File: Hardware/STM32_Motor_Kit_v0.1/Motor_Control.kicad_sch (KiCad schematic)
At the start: 138 parts, among them J4 Conn_01x03_Male, Q1 NTMFS4119NT1G, Q2 NTMFS4119NT1G, Q3 NTMFS4119NT1G, Q4 NTMFS4119NT1G, Q5 NTMFS4119NT1G, Q6 NTMFS4119NT1G, U10 LMV358IDRG4, U11 LMV358IDRG4, U12 LMV358IDRG4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

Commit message: Added GND polygon to Inner Layer-1
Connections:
- net +15V: now also JP5.2 (B), JP6.2 (B), JP7.2 (B); no longer JP5.1 (A), JP6.1 (A), JP7.1 (A)
- net at C44.1, C47.1, C50.1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: now also JP7.1 (A); no longer JP7.2 (B)
- net at C43.1, C46.1, C49.1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: now also JP6.1 (A); no longer JP6.2 (B)
- net at C45.1, C48.1, C51.1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: now also JP5.1 (A); no longer JP5.2 (B)
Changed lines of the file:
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@@
 		(lib_id "AKE_Device:Jumper_Pinheader")
 		(at 38.1 228.6 0)
+		(mirror y)
 		(unit 1)
 		(exclude_from_sim no)
@@
 		)
 		(property "Footprint" "AKE_Pinheader_TH:PinHeader_1x02_P2.54mm_Vertical"
-			(at 43.18 233.68 0)
+			(at 33.02 233.68 0)
 			(effects
 				(font
@@
 		(lib_id "AKE_Device:Jumper_Pinheader")
 		(at 39.37 165.1 0)
+		(mirror y)
 		(unit 1)
 		(exclude_from_sim no)
@@
 		)
 		(property "Footprint" "AKE_Pinheader_TH:PinHeader_1x02_P2.54mm_Vertical"
-			(at 44.45 170.18 0)
+			(at 34.29 170.18 0)
 			(effects
 				(font
@@
 		(lib_id "AKE_Device:Jumper_Pinheader")
 		(at 39.37 101.6 0)
+		(mirror y)
 		(unit 1)
 		(exclude_from_sim no)
@@
 		)
 		(property "Footprint" "AKE_Pinheader_TH:PinHeader_1x02_P2.54mm_Vertical"
-			(at 44.45 106.68 0)
+			(at 34.29 106.68 0)
 			(effects
 				(font

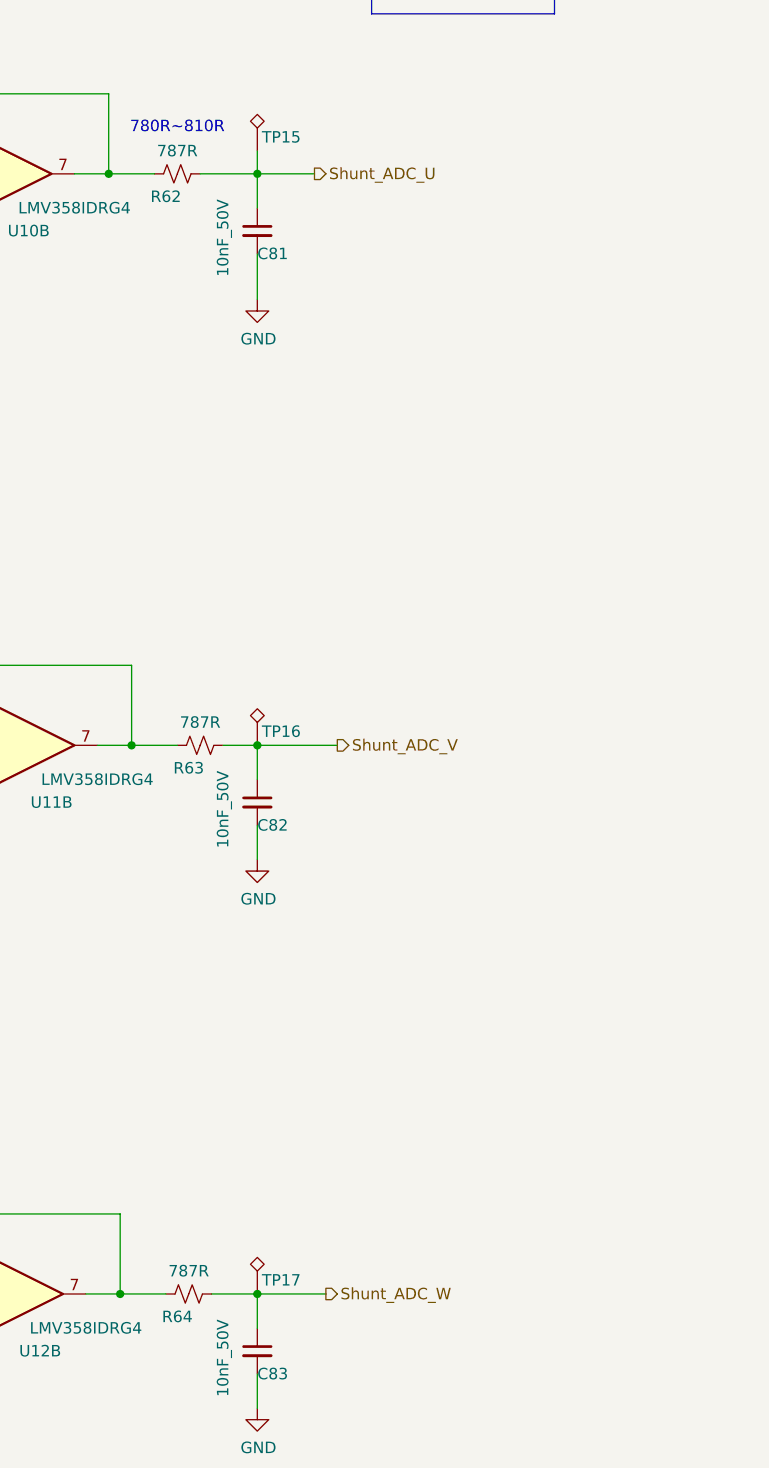
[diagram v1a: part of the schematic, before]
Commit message: Firmware Configuration added, Motor Control Pins and BackEMF Analog Pins setted.
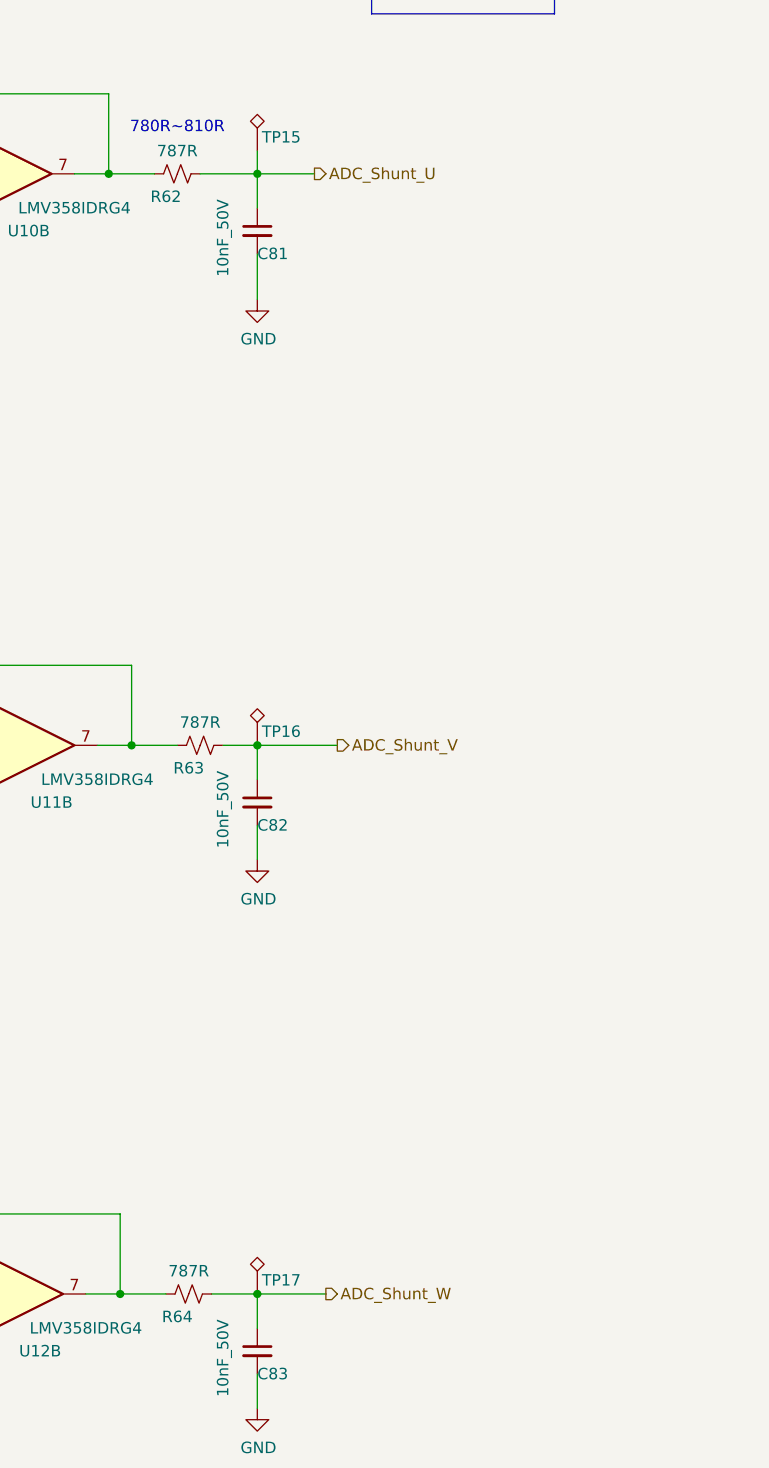
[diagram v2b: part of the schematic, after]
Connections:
- net Shunt_ADC_U renamed ADC_Shunt_U
- net Shunt_ADC_V renamed ADC_Shunt_V
- net Shunt_ADC_W renamed ADC_Shunt_W
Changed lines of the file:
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@@
 		)
 	)
-	(hierarchical_label "Shunt_ADC_V"
+	(hierarchical_label "ADC_Shunt_V"
 		(shape output)
 		(at 363.22 172.72 0)
@@
 		)
 	)
-	(hierarchical_label "Shunt_ADC_W"
+	(hierarchical_label "ADC_Shunt_W"
 		(shape output)
 		(at 361.95 233.68 0)
@@
 		)
 	)
-	(hierarchical_label "Shunt_ADC_U"
+	(hierarchical_label "ADC_Shunt_U"
 		(shape output)
 		(at 360.68 109.22 0)

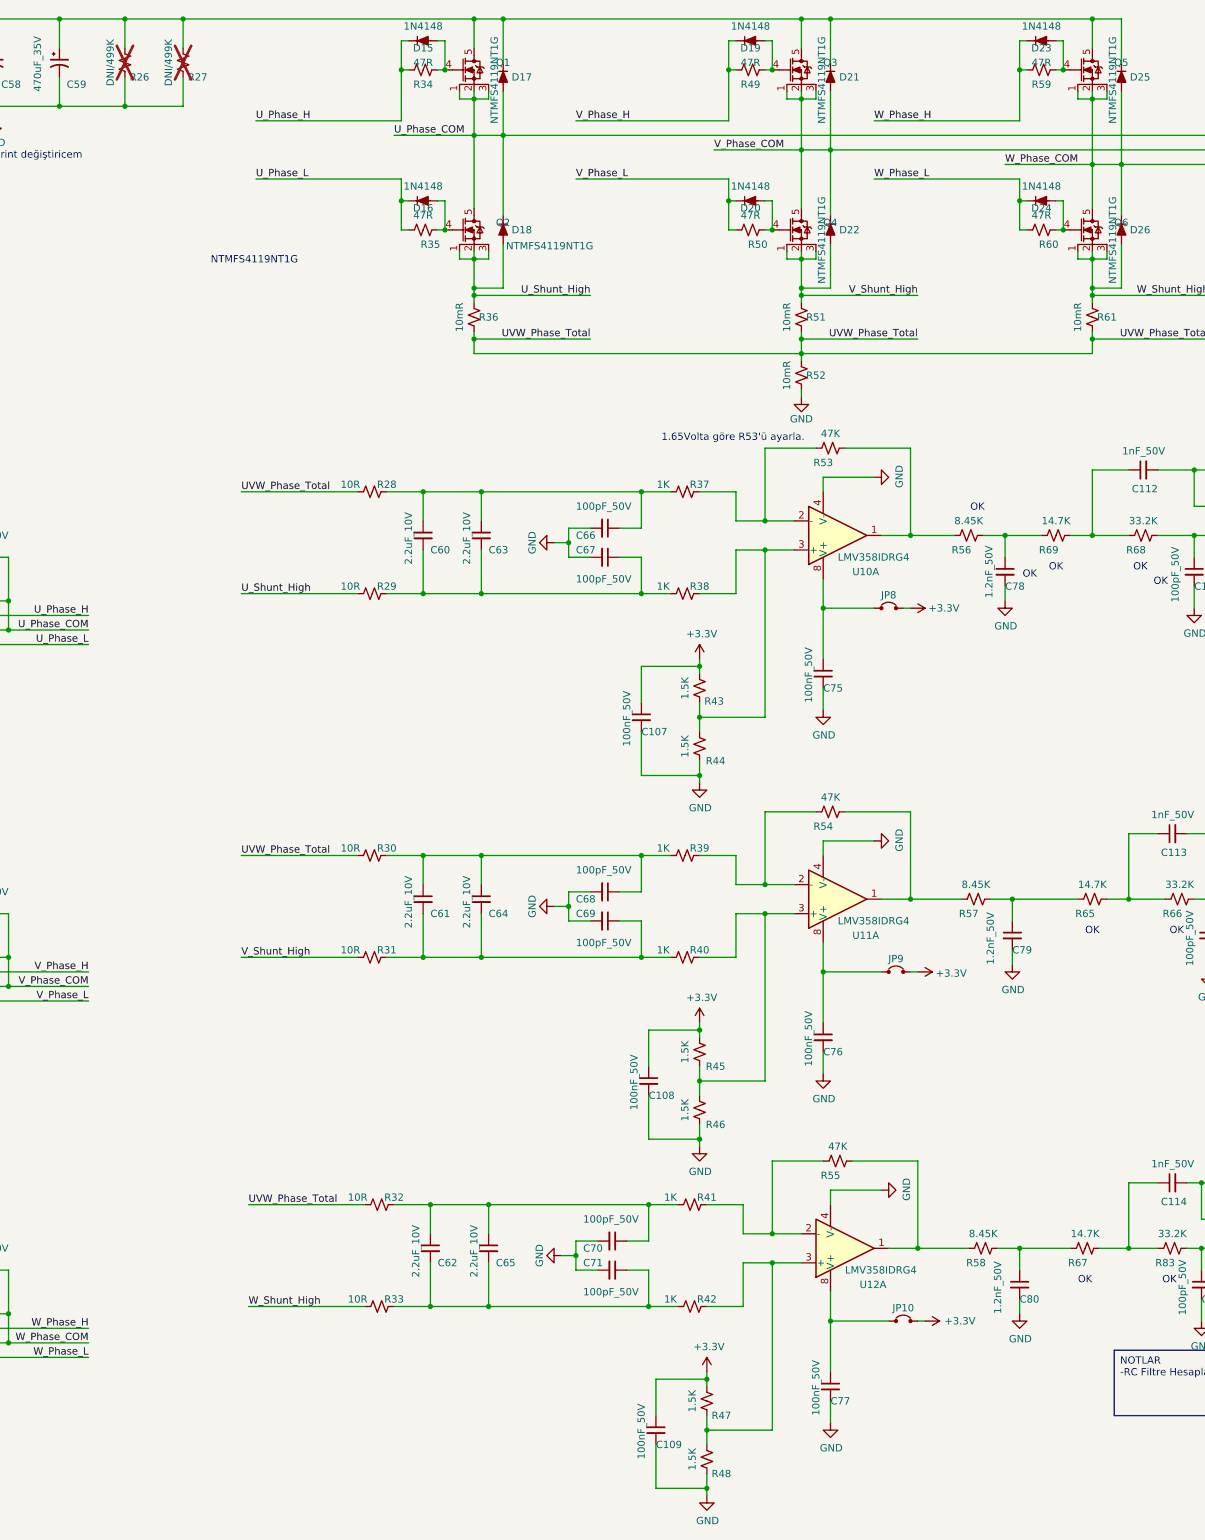
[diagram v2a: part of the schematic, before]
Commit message: Şemada güncellemeler yaptım, PCB'de revizyon yapılacak
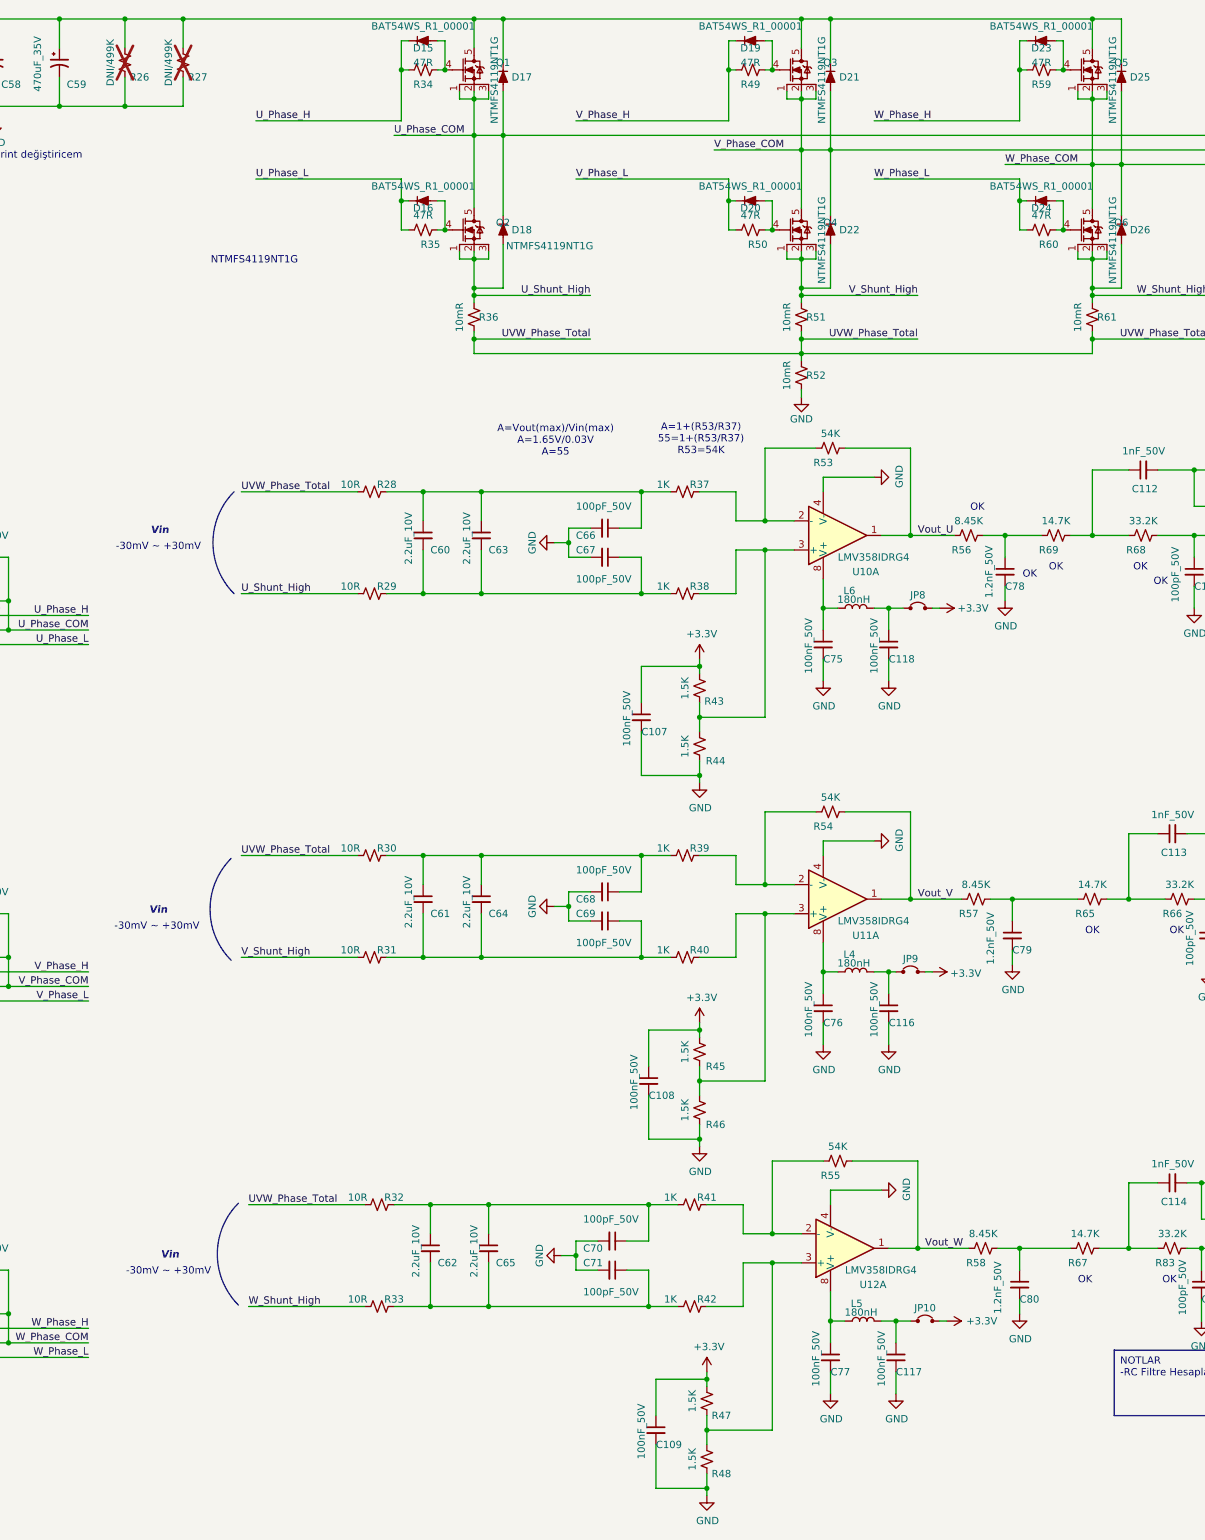
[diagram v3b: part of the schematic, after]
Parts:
- added C116, C117, C118: 100nF_50V, AKE_Capacitor_SMD:CAP_0603, symbol AKE_Capacitor:Capacitor_UnPolarised
- added L4, L5, L6: 180nH, AKE_Inductor_SMD:IND_0603, symbol AKE_Inductor:Inductor
- D15, D16, D19, D20, D23, D24: value 1N4148 -> BAT54WS_R1_00001; MFG P/N 1N4148WS_R1_00001 -> BAT54WS_R1_00001
- R53, R54, R55: value 47K -> 54K
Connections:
- net GND: now also C116.2, C117.2, C118.2
- net Vout_W: now reaches R55.1, R58.2, U12.1
- net at C77.1, U12.8 (V+): now also L5.1; no longer JP10.1 (A)
- net Vout_U: now reaches R53.1, R56.2, U10.1
- net at C75.1, U10.8 (V+): now also L6.1; no longer JP8.1 (A)
- net Vout_V: now reaches R54.1, R57.2, U11.1
- net at C76.1, U11.8 (V+): now also L4.1; no longer JP9.1 (A)
- new net: C117.1, JP10.1 (A), L5.2
- new net: C118.1, JP8.1 (A), L6.2
- new net: C116.1, JP9.1 (A), L4.2
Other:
- note added: "-30mV ~ +30mV"
- note added: "A=1+(R53/R37) 55=1+(R53/R37) R53=54K"
- note added: "A=Vout(max)/Vin(max) A=1.65V/0.03V A=55"
- note added: "Vin"
- note removed: "1.65Volta göre R53'ü ayarla."
- moved on the sheet: C75, C76, C77, JP10, JP8, JP9

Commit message: 12.01.2025
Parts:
- added C103, C119, C120, C85, C86, C87: 10nF_50V, AKE_Capacitor_SMD:CAP_0805, symbol AKE_Capacitor:Capacitor_UnPolarised
- added R112, R124, R125, R126, R127, R128: 2.4R, AKE_Resistor_SMD:RES_0805, symbol AKE_Resistor:Resistor_US
- added R118, R119, R120, R121, R122, R123: 10K, AKE_Resistor_SMD:RES_0603, symbol AKE_Resistor:Resistor_US
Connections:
- net U_Phase_COM: now also C86.1, R112.2, R118.2
- net U_Shunt_High: now also R121.2, R124.2
- net V_Phase_COM: now also C119.1, R119.2, R125.2
- net V_Shunt_High: now also R122.2, R127.2
- net Vbus: now also C103.1, C85.1, C87.1
- net W_Phase_COM: now also C120.1, R120.2, R126.2
- net W_Shunt_High: now also R123.2, R128.2
- net at D20.2, Q4.4, R50.2: now also R122.1
- net at D23.2, Q5.4, R59.2: now also R120.1
- net at D19.2, Q3.4, R49.2: now also R119.1
- net at D24.2, Q6.4, R60.2: now also R123.1
- net at D15.2, Q1.4, R34.2: now also R118.1
- net at D16.2, Q2.4, R35.2: now also R121.1
- new net: C87.2, R125.1
- new net: C85.2, R112.1
- new net: C103.2, R126.1
- new net: C119.2, R127.1
- new net: C86.2, R124.1
- new net: C120.2, R128.1
